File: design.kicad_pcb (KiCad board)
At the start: 2 copper layers, 122.6 x 97.8 mm, 155 parts, among them J301 TYPE-C-31-M-12, U1 TTP223, U10 ATtiny1616-M, U2 TTP223, U3 TTP223, U4 TTP223, U5 TTP223, U6 TTP223, U7 TTP223, U8 TTP223

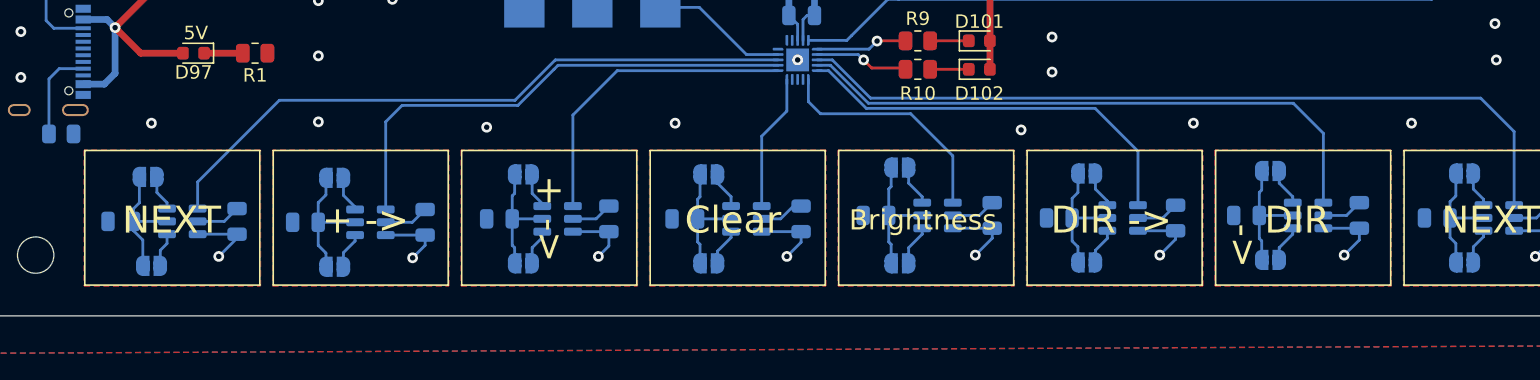
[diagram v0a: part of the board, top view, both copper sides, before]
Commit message: changed VCC to +5V and connect them
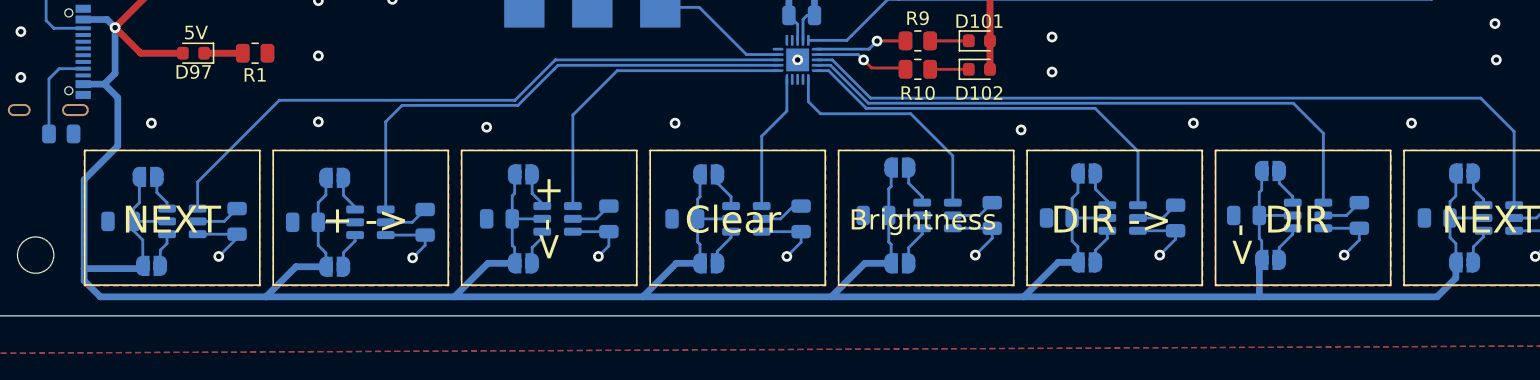
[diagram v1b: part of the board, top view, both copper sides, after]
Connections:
- C13 pad 1: VCC -> +5V
- C14 pad 1: VCC -> +5V
- C15 pad 1: VCC -> +5V
- C16 pad 1: VCC -> +5V
- C5 pad 1: VCC -> +5V
- C6 pad 1: VCC -> +5V
- C7 pad 1: VCC -> +5V
- C8 pad 1: VCC -> +5V
- JP1 pad 2: VCC -> +5V
- JP10 pad 2: VCC -> +5V
- JP11 pad 2: VCC -> +5V
- JP12 pad 2: VCC -> +5V
- JP13 pad 2: VCC -> +5V
- JP14 pad 2: VCC -> +5V
- JP15 pad 2: VCC -> +5V
- JP16 pad 2: VCC -> +5V
- JP2 pad 2: VCC -> +5V
- JP3 pad 2: VCC -> +5V
- JP4 pad 2: VCC -> +5V
- JP5 pad 2: VCC -> +5V
- JP6 pad 2: VCC -> +5V
- JP7 pad 2: VCC -> +5V
- JP8 pad 2: VCC -> +5V
- JP9 pad 2: VCC -> +5V
- U1 pad 5: VCC -> +5V
- U2 pad 5: VCC -> +5V
- U3 pad 5: VCC -> +5V
- U4 pad 5: VCC -> +5V
- U5 pad 5: VCC -> +5V
- U6 pad 5: VCC -> +5V
- U7 pad 5: VCC -> +5V
- U8 pad 5: VCC -> +5V
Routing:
- net +5V: track 308.4 -> 538.2 mm
- net VCC: track 75.6 -> 0.00 mm

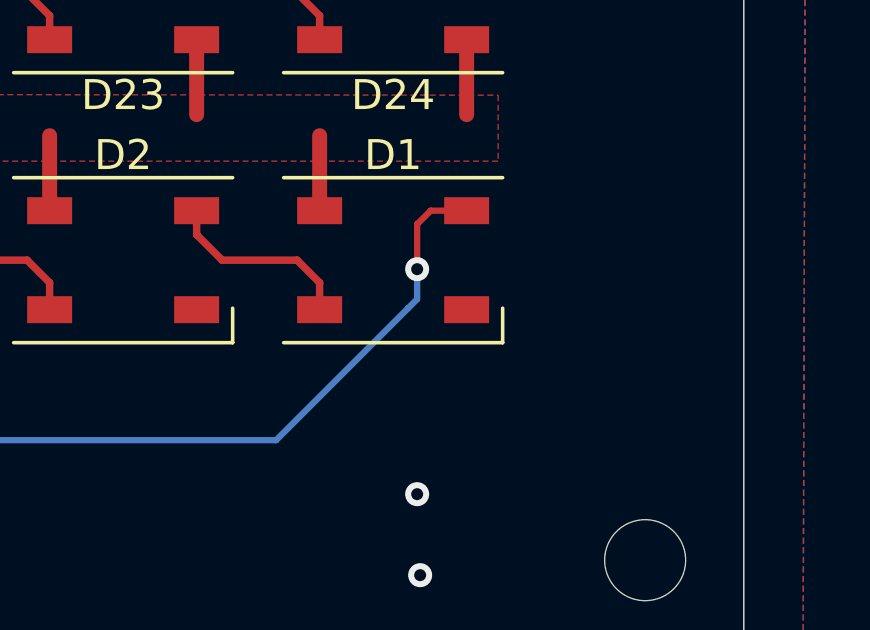
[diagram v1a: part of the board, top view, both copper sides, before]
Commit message: add series resistor
closes #2
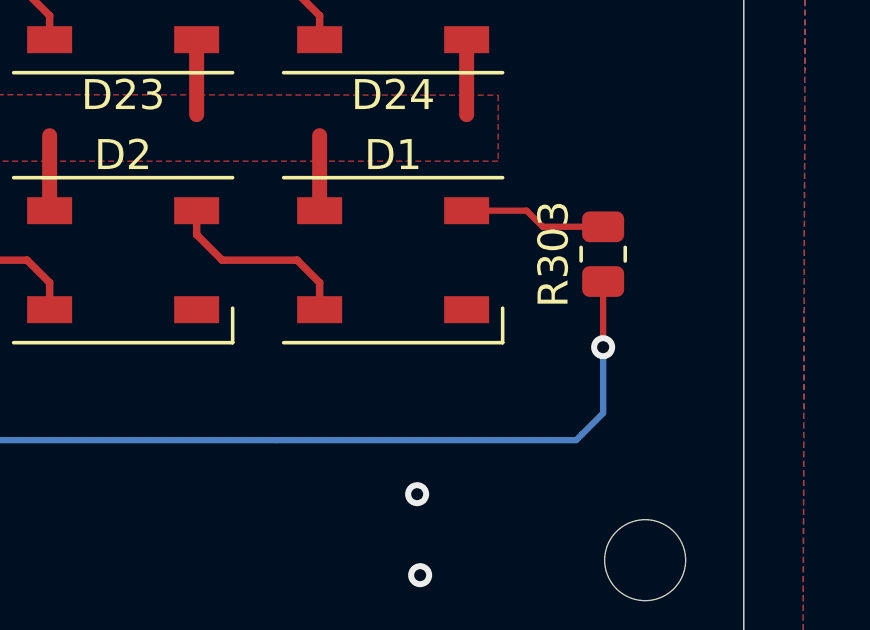
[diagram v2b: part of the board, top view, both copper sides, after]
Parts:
- added R303: 100, Resistor_SMD:R_0805_2012Metric, F.Cu at (244.3, 120.4)
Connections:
- D1 pad 4: in -> Net-(D1-Pad4)
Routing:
- net Net-(D1-Pad4): track 0.00 -> 4.77 mm
- net in: track 58.5 -> 63.2 mm

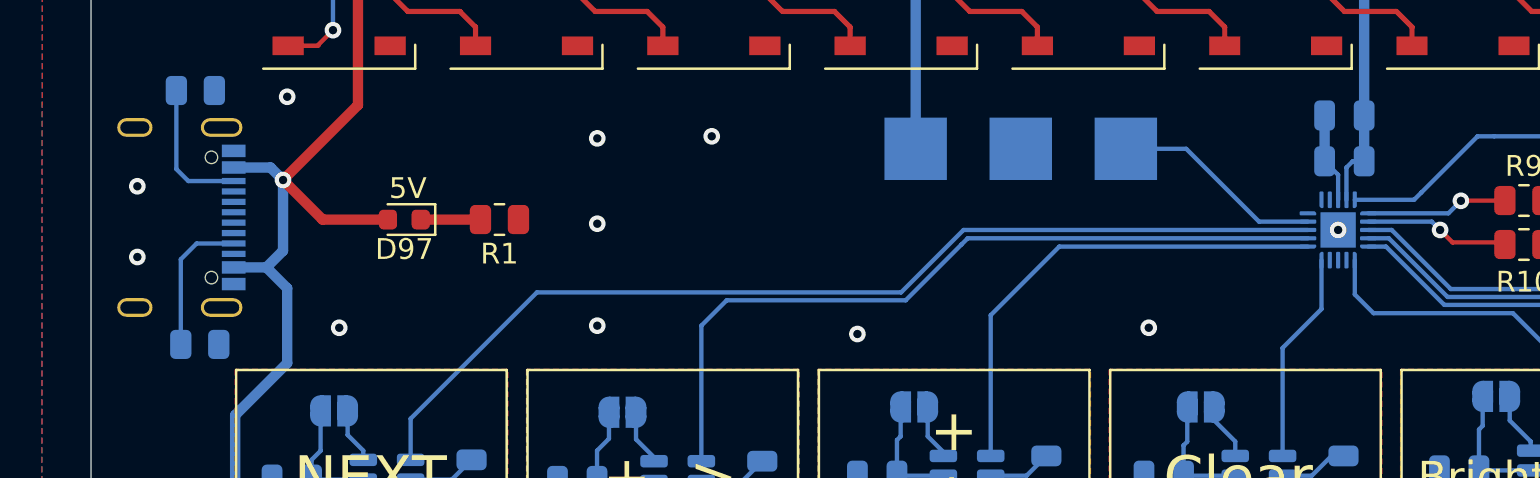
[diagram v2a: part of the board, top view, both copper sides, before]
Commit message: cange usb-c footprints soldermask. add connections to shield.
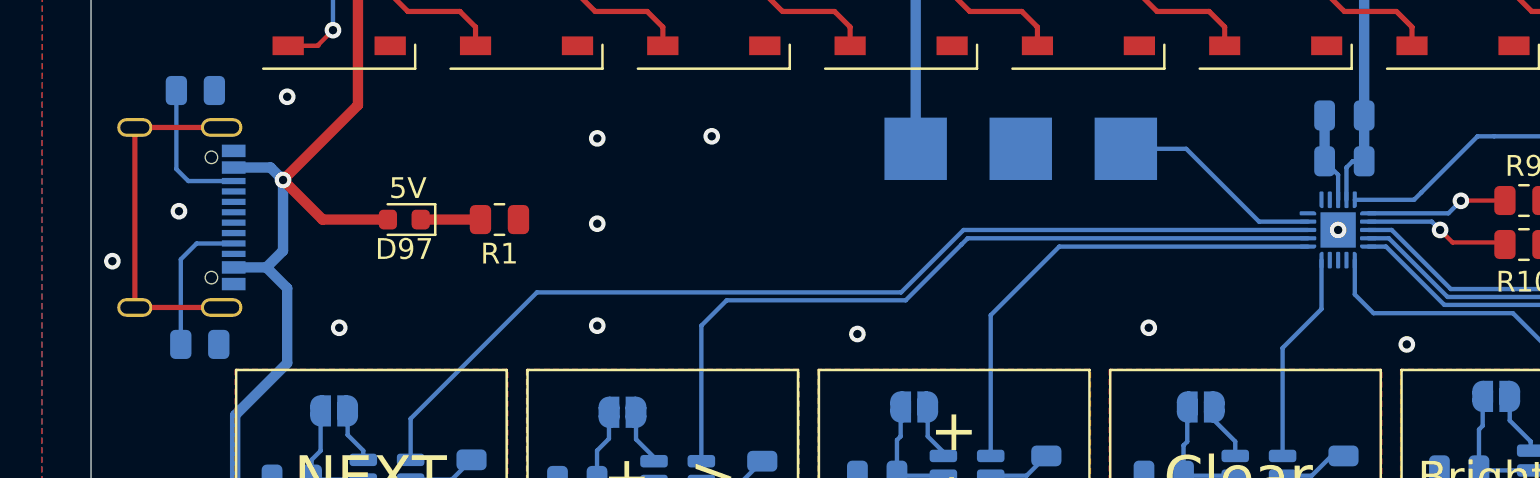
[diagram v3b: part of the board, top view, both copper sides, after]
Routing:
- net unconnected-(J301-PadS1): track 0.00 -> 17.0 mm
- net GND: vias 66 -> 67
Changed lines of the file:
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@@
       (effects (font (size 0.48 0.48) (thickness 0.15)) (justify mirror))
     )
-    (fp_line (start 4.47 -2.6) (end 4.47 -1.17) (layer "B.SilkS") (width 0.127))
     (fp_line (start 4.47 2.85) (end 4.47 1.17) (layer "B.SilkS") (width 0.127))
-    (fp_line (start -4.47 -2.6) (end -4.47 -1.17) (layer "B.SilkS") (width 0.127))
     (fp_line (start -4.47 2.85) (end -4.47 1.17) (layer "B.SilkS") (width 0.127))
-    (fp_line (start -4.47 -2.6) (end 4.47 -2.6) (layer "B.SilkS") (width 0.127))
     (fp_circle (center -3.2 6) (end -3.1 6) (layer "B.SilkS") (width 0.2) (fill none))
+    (fp_poly (pts
+        (xy 0.05 5.37)
+        (xy 0.45 5.37)
+        (xy 0.45 4.13)
+        (xy 0.05 4.13)
+      ) (layer "B.Mask") (width 0.01) (fill solid))
+    (fp_poly (pts
+        (xy 1.55 5.37)
+        (xy 1.95 5.37)
+        (xy 1.95 4.13)
+        (xy 1.55 4.13)
+      ) (layer "B.Mask") (width 0.01) (fill solid))
+    (fp_poly (pts
+        (xy 2.05 5.37)
+        (xy 2.75 5.37)
+        (xy 2.75 4.13)
+        (xy 2.05 4.13)
+      ) (layer "B.Mask") (width 0.01) (fill solid))
+    (fp_poly (pts
+        (xy -1.45 5.37)
+        (xy -1.05 5.37)
+        (xy -1.05 4.13)
+        (xy -1.45 4.13)
+      ) (layer "B.Mask") (width 0.01) (fill solid))
     (fp_poly (pts
         (xy -2.75 5.37)
@@
         (xy -2.05 4.13)
         (xy -2.75 4.13)
+      ) (layer "B.Mask") (width 0.01) (fill solid))
+    (fp_poly (pts
+        (xy -0.45 5.37)
+        (xy -0.05 5.37)
+        (xy -0.05 4.13)
+        (xy -0.45 4.13)
+      ) (layer "B.Mask") (width 0.01) (fill solid))
+    (fp_poly (pts
+        (xy -1.95 5.37)
+        (xy -1.55 5.37)
+        (xy -1.55 4.13)
+        (xy -1.95 4.13)
       ) (layer "B.Mask") (width 0.01) (fill solid))
     (fp_poly (pts
@@
       ) (layer "B.Mask") (width 0.01) (fill solid))
     (fp_poly (pts
-        (xy 1.55 5.37)
-        (xy 1.95 5.37)
-        (xy 1.95 4.13)
-        (xy 1.55 4.13)
-      ) (layer "B.Mask") (width 0.01) (fill solid))
-    (fp_poly (pts
-        (xy -1.45 5.37)
-        (xy -1.05 5.37)
-        (xy -1.05 4.13)
-        (xy -1.45 4.13)
-      ) (layer "B.Mask") (width 0.01) (fill solid))
-    (fp_poly (pts
-        (xy -1.95 5.37)
-        (xy -1.55 5.37)
-        (xy -1.55 4.13)
-        (xy -1.95 4.13)
-      ) (layer "B.Mask") (width 0.01) (fill solid))
-    (fp_poly (pts
-        (xy -0.45 5.37)
-        (xy -0.05 5.37)
-        (xy -0.05 4.13)
-        (xy -0.45 4.13)
+        (xy -3.55 5.37)
+        (xy -2.85 5.37)
+        (xy -2.85 4.13)
+        (xy -3.55 4.13)
       ) (layer "B.Mask") (width 0.01) (fill solid))
     (fp_poly (pts
@@
       ) (layer "B.Mask") (width 0.01) (fill solid))
     (fp_poly (pts
-        (xy 0.05 5.37)
-        (xy 0.45 5.37)
-        (xy 0.45 4.13)
-        (xy 0.05 4.13)
+        (xy -0.95 5.37)
+        (xy -0.55 5.37)
+        (xy -0.55 4.13)
+        (xy -0.95 4.13)
       ) (layer "B.Mask") (width 0.01) (fill solid))
     (fp_poly (pts
@@
         (xy 1.05 4.13)
       ) (layer "B.Mask") (width 0.01) (fill solid))
-    (fp_poly (pts
-        (xy 2.05 5.37)
-        (xy 2.75 5.37)
-        (xy 2.75 4.13)
-        (xy 2.05 4.13)
-      ) (layer "B.Mask") (width 0.01) (fill solid))
-    (fp_poly (pts
-        (xy -0.95 5.37)
-        (xy -0.55 5.37)
-        (xy -0.55 4.13)
-        (xy -0.95 4.13)
-      ) (layer "B.Mask") (width 0.01) (fill solid))
-    (fp_poly (pts
-        (xy -3.55 5.37)
-        (xy -2.85 5.37)
-        (xy -2.85 4.13)
-        (xy -3.55 4.13)
-      ) (layer "B.Mask") (width 0.01) (fill solid))
+    (fp_line (start 5.025 5.57) (end -5.025 5.57) (layer "B.CrtYd") (width 0.05))
+    (fp_line (start -5.025 -2.85) (end 5.025 -2.85) (layer "B.CrtYd") (width 0.05))
     (fp_line (start 5.025 -2.85) (end 5.025 5.57) (layer "B.CrtYd") (width 0.05))
-    (fp_line (start -5.025 -2.85) (end 5.025 -2.85) (layer "B.CrtYd") (width 0.05))
-    (fp_line (start 5.025 5.57) (end -5.025 5.57) (layer "B.CrtYd") (width 0.05))
     (fp_line (start -5.025 5.57) (end -5.025 -2.85) (layer "B.CrtYd") (width 0.05))
-    (fp_line (start -4.47 -2.6) (end 4.47 -2.6) (layer "B.Fab") (width 0.127))
-    (fp_line (start 4.47 4.75) (end -4.47 4.75) (layer "B.Fab") (width 0.127))
     (fp_line (start -5.5 -2.11) (end 9 -2.11) (layer "B.Fab") (width 0.127))
     (fp_line (start 4.47 -2.6) (end 4.47 4.75) (layer "B.Fab") (width 0.127))
     (fp_line (start -4.47 4.75) (end -4.47 -2.6) (layer "B.Fab") (width 0.127))
+    (fp_line (start -4.47 -2.6) (end 4.47 -2.6) (layer "B.Fab") (width 0.127))
+    (fp_line (start 4.47 -2.6) (end 4.47 -1.17) (layer "B.Fab") (width 0.127))
+    (fp_line (start -4.47 -2.6) (end 4.47 -2.6) (layer "B.Fab") (width 0.127))
+    (fp_line (start -4.47 -2.6) (end -4.47 -1.17) (layer "B.Fab") (width 0.127))
+    (fp_line (start 4.47 4.75) (end -4.47 4.75) (layer "B.Fab") (width 0.127))
     (fp_circle (center -3.2 6) (end -3.1 6) (layer "B.Fab") (width 0.2) (fill none))
+    (pad "" np_thru_hole circle (at -2.89 3.68 90) (size 0.6 0.6) (drill 0.6) (layers *.Cu *.Mask))
     (pad "" np_thru_hole circle (at 2.89 3.68 90) (size 0.6 0.6) (drill 0.6) (layers *.Cu *.Mask))
-    (pad "" np_thru_hole circle (at -2.89 3.68 90) (size 0.6 0.6) (drill 0.6) (layers *.Cu *.Mask))
     (pad "A1_B12" smd rect (at -3.2 4.75 90) (size 0.6 1.14) (layers "B.Cu" "B.Paste")
       (net 2 "GND") (pinfunction "GND") (pintype "power_in"))
@@
   (via (at 228.3 89.2) (size 0.8) (drill 0.4) (layers "F.Cu" "B.Cu") (free) (net 2))
   (via (at 228.3 107) (size 0.8) (drill 0.4) (layers "F.Cu" "B.Cu") (free) (net 2))
-  (via (at 128.6 132.4) (size 0.8) (drill 0.4) (layers "F.Cu" "B.Cu") (free) (net 2))
+  (via (at 127.4 132.6) (size 0.8) (drill 0.4) (layers "F.Cu" "B.Cu") (free) (net 2))
   (via (at 201.7 54.3) (size 0.8) (drill 0.4) (layers "F.Cu" "B.Cu") (free) (net 2))
-  (via (at 128.6 129) (size 0.8) (drill 0.4) (layers "F.Cu" "B.Cu") (free) (net 2))
+  (via (at 130.6 130.2) (size 0.8) (drill 0.4) (layers "F.Cu" "B.Cu") (free) (net 2))
   (via (at 201.3 89.2) (size 0.8) (drill 0.4) (layers "F.Cu" "B.Cu") (free) (net 2))
   (via (at 205.2 132) (size 0.8) (drill 0.4) (layers "F.Cu" "B.Cu") (free) (net 2))
@@
   (via (at 219.3 54.3) (size 0.8) (drill 0.4) (layers "F.Cu" "B.Cu") (free) (net 2))
   (via (at 173.6 89.2) (size 0.8) (drill 0.4) (layers "F.Cu" "B.Cu") (free) (net 2))
+  (via (at 189.6 136.6) (size 0.8) (drill 0.4) (layers "F.Cu" "B.Cu") (free) (net 2))
   (via (at 210 89.2) (size 0.8) (drill 0.4) (layers "F.Cu" "B.Cu") (free) (net 2))
   (via (at 210.4 54.3) (size 0.8) (drill 0.4) (layers "F.Cu" "B.Cu") (free) (net 2))
@@
   (segment (start 130.475 128.175) (end 131.05 128.75) (width 0.21) (layer "B.Cu") (net 149))
   (segment (start 130.475 124.4) (end 130.475 128.175) (width 0.21) (layer "B.Cu") (net 149))
+  (segment (start 128.48 134.825) (end 128.48 126.175) (width 0.25) (layer "F.Cu") (net 153))
+  (segment (start 128.48 126.175) (end 132.65 126.175) (width 0.25) (layer "F.Cu") (net 153))
+  (segment (start 128.48 134.825) (end 132.65 134.825) (width 0.25) (layer "F.Cu") (net 153))
   (zone (net 8) (net_name "touch_point_8") (layer "F.Cu") (hatch edge 0.508)
     (priority 1)
